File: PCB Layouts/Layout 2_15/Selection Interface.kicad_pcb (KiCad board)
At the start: 4 copper layers, 110 x 90 mm, 127 parts, among them P13 CONN_01X10, P18 CONN_02X05, P19 CONN_02X05, P21 CONN_02X05, P6 CONN_02X10, P8 CONN_02X04, U1 CY8C42_(48_TQFP), U2 CY8C42_(48_TQFP), U3 CY8C58_(100_TQFP), U3_USB USB_2.0_B, U4 CY8C42_(48_TQFP), U5 68_PLCC_Socket_(8468-21B1-RK-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, U6 CY8C42_(48_TQFP), U7 CY8C58_(100_TQFP), U7_USB USB_2.0_B

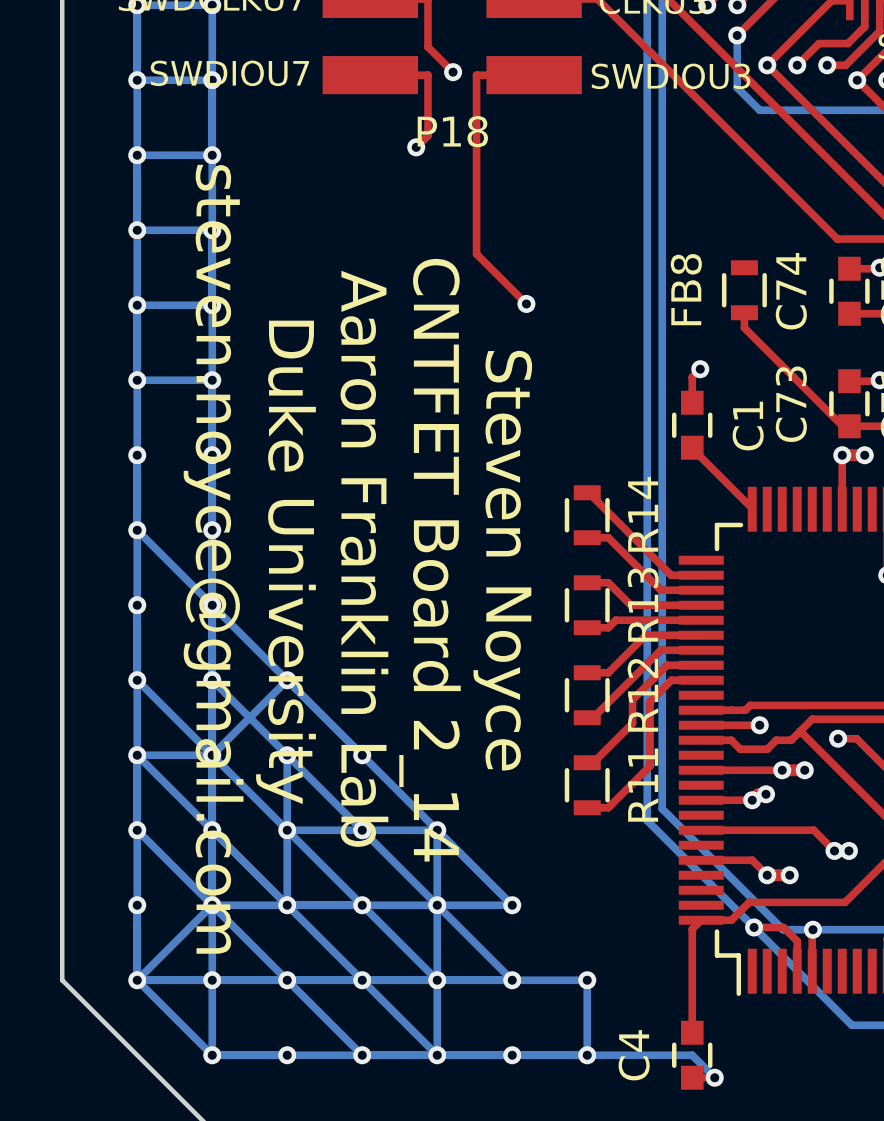
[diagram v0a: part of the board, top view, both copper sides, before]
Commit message: Loaded and updated PCB Layout 2_15 for the first time
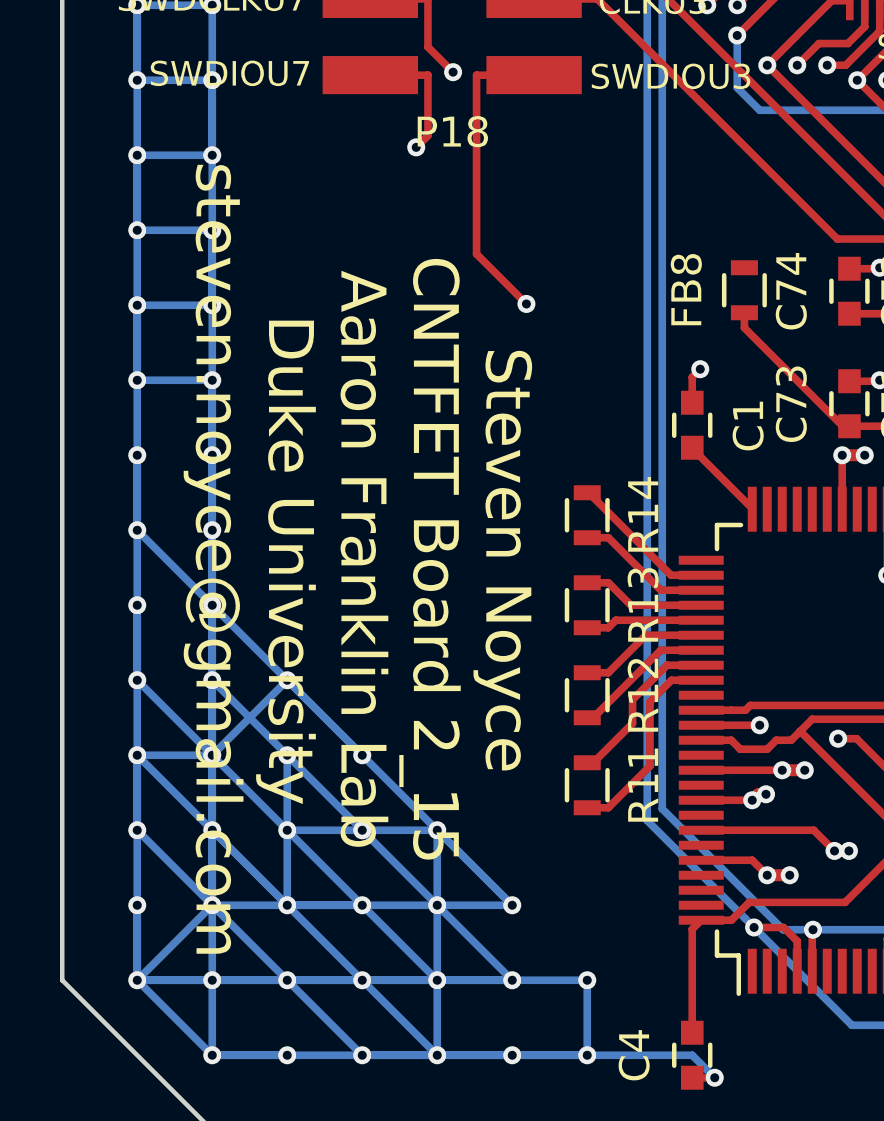
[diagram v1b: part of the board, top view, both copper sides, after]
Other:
- board text added: "Steven Noyce CNTFET Board 2_15 Aaron Franklin Lab Duke University steven.noyce@gmail.com"
- board text removed: "Steven Noyce CNTFET Board 2_14 Aaron Franklin Lab Duke University steven.noyce@gmail.com"
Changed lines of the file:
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@@
-(kicad_pcb (version 4) (host pcbnew 4.0.5)
+(kicad_pcb (version 20171130) (host pcbnew "(5.0.0-3-g5ebb6b6)")
   (general
-    (links 505)
-    (no_connects 0)
-    (area 97.599999 -10.100001 283.600001 200.100001)
     (thickness 1.6)
     (drawings 129)
@@
       (layerselection 0x010f8_80000007)
       (usegerberextensions false)
+      (usegerberattributes false)
+      (usegerberadvancedattributes false)
+      (creategerberjobfile false)
       (excludeedgelayer true)
       (linewidth 0.100000)
@@
       (hpglpennumber 1)
       (hpglpenspeed 20)
-      (hpglpendiameter 15)
-      (hpglpenoverlay 2)
+      (hpglpendiameter 15.000000)
       (psnegative false)
       (psa4output false)
@@
       (drillshape 0)
       (scaleselection 1)
-      (outputdirectory Gerbers/))
+      (outputdirectory "Gerbers/"))
   )
   (net 0 "")
@@
     (solder_paste_ratio -0.16)
     (attr smd)
-    (fp_text reference U2 (at -5.9 0 360) (layer F.SilkS)
+    (fp_text reference U2 (at -5.9 0) (layer F.SilkS)
       (effects (font (size 1 1) (thickness 0.15)))
     )
@@
     (solder_mask_margin 0.2)
     (solder_paste_margin -0.1)
-    (fp_text reference P6 (at -13.31 0 360) (layer F.SilkS)
+    (fp_text reference P6 (at -13.31 0) (layer F.SilkS)
       (effects (font (size 1 1) (thickness 0.15)))
     )
@@
     (solder_mask_margin 0.2)
     (solder_paste_margin -0.1)
-    (fp_text reference P19 (at 7 0 360) (layer F.SilkS)
+    (fp_text reference P19 (at 7 0) (layer F.SilkS)
       (effects (font (size 1 1) (thickness 0.15)))
     )
@@
     (solder_mask_margin 0.2)
     (solder_paste_margin -0.1)
-    (fp_text reference P21 (at -7 0 360) (layer F.SilkS)
+    (fp_text reference P21 (at -7 0) (layer F.SilkS)
       (effects (font (size 1 1) (thickness 0.15)))
     )
@@
     (solder_mask_margin 0.2)
     (solder_paste_margin -0.1)
-    (fp_text reference P13 (at -13.23 0 360) (layer F.SilkS)
+    (fp_text reference P13 (at -13.23 0) (layer F.SilkS)
       (effects (font (size 1 1) (thickness 0.15)))
     )
@@
   (gr_line (start 206 159) (end 194 159) (angle 90) (layer Edge.Cuts) (width 0.15))
   (gr_line (start 207 160) (end 206 159) (angle 90) (layer Edge.Cuts) (width 0.15))
-  (gr_text "Steven Noyce\nCNTFET Board 2_14\nAaron Franklin Lab\nDuke University\nsteven.noyce@gmail.com" (at 160 141 270) (layer F.SilkS)
+  (gr_text "Steven Noyce\nCNTFET Board 2_15\nAaron Franklin Lab\nDuke University\nsteven.noyce@gmail.com" (at 160 141 270) (layer F.SilkS)
     (effects (font (size 1.5 1.5) (thickness 0.3)))
   )

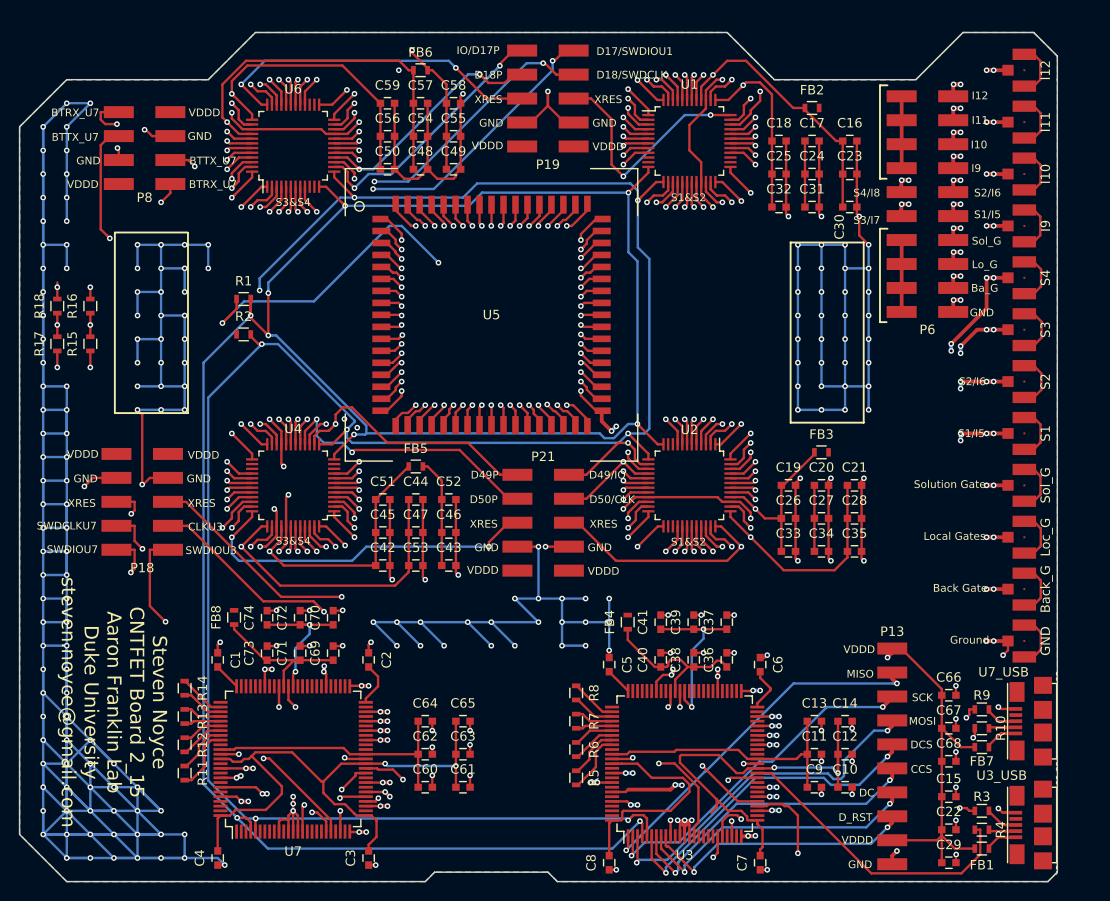
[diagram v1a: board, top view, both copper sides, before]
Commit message: Regenerated and loaded the netlist for Layout 2_15. All components are now switched over to the most up-to-date footprints. Added mounting holes to the schematic and layout. The design is now ready for a more significant overhaul, so will likely be creating a new version soon.
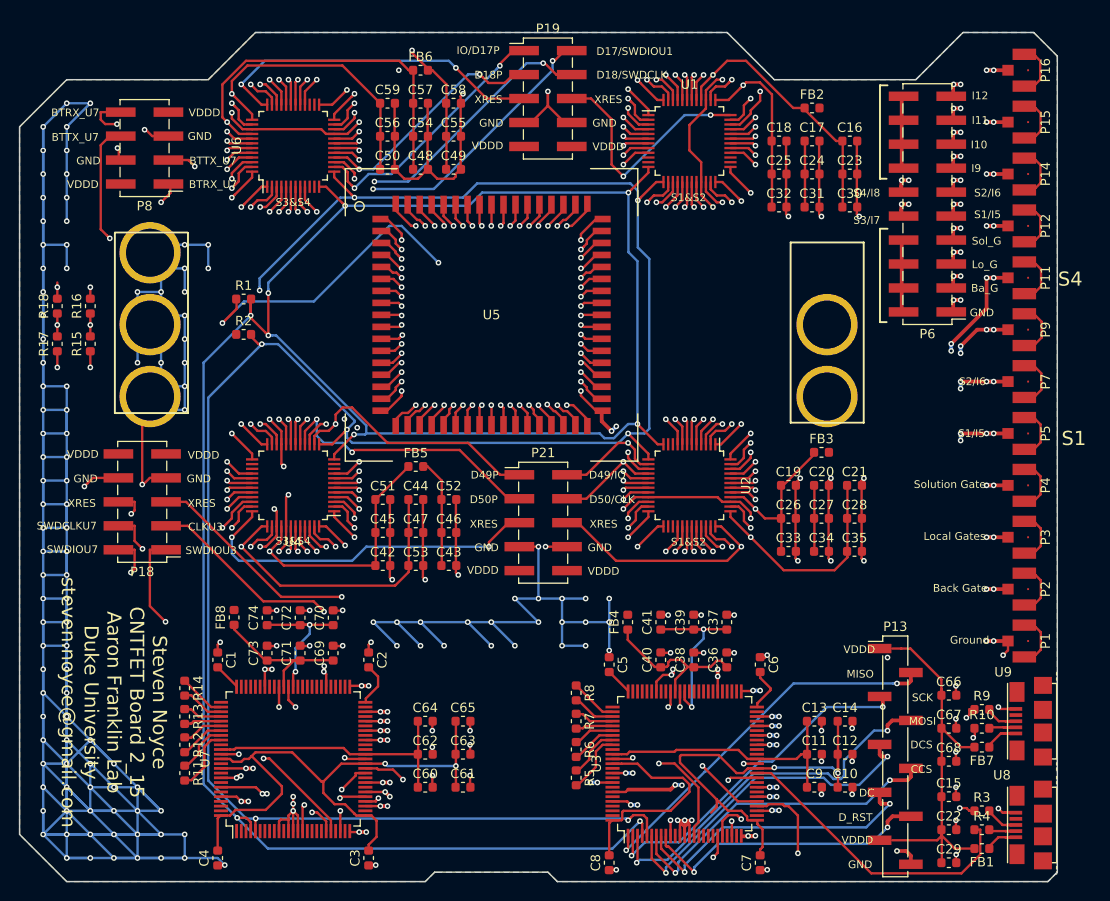
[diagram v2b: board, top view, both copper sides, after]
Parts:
- removed Back_G, GND, I10, I11, I12, I9, Loc_G, S1, S2, S3, S4, Sol_G: CONN_01X02, NoyceLibrary:IPEX_Connector_SMD_(RECE.20279.001E.01)
- removed U3_USB, U7_USB: USB_2.0_B, NoyceLibrary:Micro_USB_2.0_B_SMD(10118192-0001LF)
- added MH1: MountingHole, Custom_Footprint_Library:MountingHole_5.1mm, F.Cu at (163.8, 92.7)
- added MH2: MountingHole, Custom_Footprint_Library:MountingHole_5.1mm, F.Cu at (163.8, 100.3)
- added MH3: MountingHole, Custom_Footprint_Library:MountingHole_5.1mm, F.Cu at (163.8, 108.0)
- added MH5: MountingHole, Custom_Footprint_Library:MountingHole_5.1mm, F.Cu at (236.2, 103.5)
- added MH6: MountingHole, Custom_Footprint_Library:MountingHole_5.1mm, F.Cu at (236.2, 108.6)
- added P1: CONN_01X02, Custom_Footprint_Library:IPEX_Connector_SMD_(RECE.20279.001E.01), F.Cu at (255.2, 134.5)
- added P11: CONN_01X02, Custom_Footprint_Library:IPEX_Connector_SMD_(RECE.20279.001E.01), F.Cu at (255.2, 96.0)
- added P12: CONN_01X02, Custom_Footprint_Library:IPEX_Connector_SMD_(RECE.20279.001E.01), F.Cu at (255.2, 90.5)
- added P14: CONN_01X02, Custom_Footprint_Library:IPEX_Connector_SMD_(RECE.20279.001E.01), F.Cu at (255.2, 85.0)
- added P15: CONN_01X02, Custom_Footprint_Library:IPEX_Connector_SMD_(RECE.20279.001E.01), F.Cu at (255.2, 79.5)
- added P16: CONN_01X02, Custom_Footprint_Library:IPEX_Connector_SMD_(RECE.20279.001E.01), F.Cu at (255.2, 74.0)
- added P2: CONN_01X02, Custom_Footprint_Library:IPEX_Connector_SMD_(RECE.20279.001E.01), F.Cu at (255.2, 129.0)
- added P3: CONN_01X02, Custom_Footprint_Library:IPEX_Connector_SMD_(RECE.20279.001E.01), F.Cu at (255.2, 123.5)
- added P4: CONN_01X02, Custom_Footprint_Library:IPEX_Connector_SMD_(RECE.20279.001E.01), F.Cu at (255.2, 118.0)
- added P5: CONN_01X02, Custom_Footprint_Library:IPEX_Connector_SMD_(RECE.20279.001E.01), F.Cu at (255.2, 112.5)
- added P7: CONN_01X02, Custom_Footprint_Library:IPEX_Connector_SMD_(RECE.20279.001E.01), F.Cu at (255.2, 107.0)
- added P9: CONN_01X02, Custom_Footprint_Library:IPEX_Connector_SMD_(RECE.20279.001E.01), F.Cu at (255.2, 101.5)
- added U8: USB_2.0_B, Custom_Footprint_Library:Micro_USB_2.0_B_SMD(10118192-0001LF), F.Cu at (258.5, 154.0)
- added U9: USB_2.0_B, Custom_Footprint_Library:Micro_USB_2.0_B_SMD(10118192-0001LF), F.Cu at (258.5, 143.0)
- C1, C10, C11, C12, C13, C14, C15, C16, C17, C18, C19, C2, C20, C21, C22, C23, C24, C25, C26, C27, C28, C29, C3, C30, C31, C32, C33, C34, C35, C36, C37, C38, C39, C4, C40, C41, C42, C43, C44, C45, C46, C47, C48, C49, C5, C50, C51, C52, C53, C54, C55, C56, C57, C58, C59, C6, C60, C61, C62, C63, C64, C65, C66, C67, C68, C69, C7, C70, C71, C72, C73, C74, C8, C9: footprint Capacitors_SMD:C_0603 -> Capacitor_SMD:C_0603_1608Metric
- FB1, FB2, FB3, FB4, FB5, FB6, FB7, FB8, R1, R10, R11, R12, R13, R14, R15, R16, R17, R18, R2, R3, R4, R5, R6, R7, R8, R9: footprint Resistors_SMD:R_0603 -> Resistor_SMD:R_0603_1608Metric
- P13: footprint NoyceLibrary:Headers_SMD_1x10_(cut_95157-240LF) -> Connector_PinHeader_2.54mm:PinHeader_1x10_P2.54mm_Vertical_SMD_Pin1Left
- P18, P19, P21: footprint NoyceLibrary:Headers_SMD_2x5_(cut_95157-240LF) -> Connector_PinHeader_2.54mm:PinHeader_2x05_P2.54mm_Vertical_SMD
- P6: footprint NoyceLibrary:Headers_SMD_2x10_(cut_95157-240LF) -> Connector_PinHeader_2.54mm:PinHeader_2x10_P2.54mm_Vertical_SMD
- P8: footprint NoyceLibrary:Headers_SMD_2x4_(cut_95157-240LF) -> Connector_PinHeader_2.54mm:PinHeader_2x04_P2.54mm_Vertical_SMD
- U1, U2, U4, U6: footprint Housings_QFP:TQFP-48_7x7mm_Pitch0.5mm -> Package_QFP:TQFP-48_7x7mm_P0.5mm
- U3, U7: footprint Housings_QFP:TQFP-100_14x14mm_Pitch0.5mm -> Package_QFP:TQFP-100_14x14mm_P0.5mm
- U5: footprint NoyceLibrary:68_PLCC_Socket_(8468-21B1-RK-TP) -> Custom_Footprint_Library:68_PLCC_Socket_(8468-21B1-RK-TP)
- moved P13 0.32 mm to (242.8, 146.7), turned to 0 degrees
- turned P18 to 180 degrees
- turned P19 to 0 degrees
- turned P21 to 0 degrees
- turned P6 to 180 degrees
- turned P8 to 180 degrees
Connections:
- U1 pad 10: (no net) -> Net-(U1-Pad10)
- U1 pad 11: (no net) -> Net-(U1-Pad11)
- U1 pad 26: (no net) -> Net-(U1-Pad26)
- U1 pad 27: (no net) -> Net-(U1-Pad27)
- U2 pad 10: (no net) -> Net-(U2-Pad10)
- U2 pad 11: (no net) -> Net-(U2-Pad11)
- U2 pad 26: (no net) -> Net-(U2-Pad26)
- U2 pad 27: (no net) -> Net-(U2-Pad27)
- U3 pad 11: (no net) -> Net-(U3-Pad11)
- U3 pad 16: (no net) -> Net-(U3-Pad16)
- U3 pad 17: (no net) -> Net-(U3-Pad17)
- U3 pad 18: (no net) -> Net-(U3-Pad18)
- U3 pad 19: (no net) -> Net-(U3-Pad19)
- U3 pad 22: (no net) -> Net-(U3-Pad22)
- U3 pad 24: (no net) -> Net-(U3-Pad24)
- U3 pad 27: (no net) -> Net-(U3-Pad27)
- U3 pad 32: (no net) -> Net-(U3-Pad32)
- U3 pad 34: (no net) -> Net-(U3-Pad34)
- U3 pad 40: (no net) -> Net-(U3-Pad40)
- U3 pad 41: (no net) -> Net-(U3-Pad41)
- U3 pad 43: (no net) -> Net-(U3-Pad43)
- U3 pad 45: (no net) -> Net-(U3-Pad45)
- U3 pad 47: (no net) -> Net-(U3-Pad47)
- U3 pad 49: (no net) -> Net-(U3-Pad49)
- U3 pad 52: (no net) -> Net-(U3-Pad52)
- U3 pad 53: (no net) -> Net-(U3-Pad53)
- U3 pad 54: (no net) -> Net-(U3-Pad54)
- U3 pad 55: (no net) -> Net-(U3-Pad55)
- U3 pad 57: (no net) -> Net-(U3-Pad57)
- U3 pad 58: (no net) -> Net-(U3-Pad58)
- U3 pad 59: (no net) -> Net-(U3-Pad59)
- U3 pad 60: (no net) -> Net-(U3-Pad60)
- U3 pad 61: (no net) -> Net-(U3-Pad61)
- U3 pad 62: (no net) -> Net-(U3-Pad62)
- U3 pad 67: (no net) -> Net-(U3-Pad67)
- U3 pad 68: (no net) -> Net-(U3-Pad68)
- U3 pad 70: (no net) -> Net-(U3-Pad70)
- U3 pad 71: (no net) -> Net-(U3-Pad71)
- U3 pad 72: (no net) -> Net-(U3-Pad72)
- U3 pad 73: (no net) -> Net-(U3-Pad73)
- U3 pad 74: (no net) -> Net-(U3-Pad74)
- U3 pad 76: (no net) -> Net-(U3-Pad76)
- U3 pad 85: (no net) -> Net-(U3-Pad85)
- U3 pad 89: (no net) -> Net-(U3-Pad89)
- U3 pad 91: (no net) -> Net-(U3-Pad91)
- U3 pad 93: (no net) -> Net-(U3-Pad93)
- U3 pad 95: (no net) -> Net-(U3-Pad95)
- U3 pad 97: (no net) -> Net-(U3-Pad97)
- U3 pad 98: (no net) -> Net-(U3-Pad98)
- U3 pad 99: (no net) -> Net-(U3-Pad99)
- U4 pad 10: (no net) -> Net-(U4-Pad10)
- U4 pad 11: (no net) -> Net-(U4-Pad11)
- U4 pad 26: (no net) -> Net-(U4-Pad26)
- U4 pad 27: (no net) -> Net-(U4-Pad27)
- U6 pad 10: (no net) -> Net-(U6-Pad10)
- U6 pad 11: (no net) -> Net-(U6-Pad11)
- U6 pad 26: (no net) -> Net-(U6-Pad26)
- U6 pad 27: (no net) -> Net-(U6-Pad27)
- U7 pad 1: (no net) -> Net-(U7-Pad1)
- U7 pad 11: (no net) -> Net-(U7-Pad11)
- U7 pad 16: (no net) -> Net-(U7-Pad16)
- U7 pad 17: (no net) -> Net-(U7-Pad17)
- U7 pad 18: (no net) -> Net-(U7-Pad18)
- U7 pad 19: (no net) -> Net-(U7-Pad19)
- U7 pad 2: (no net) -> Net-(U7-Pad2)
- U7 pad 22: (no net) -> Net-(U7-Pad22)
- U7 pad 24: (no net) -> Net-(U7-Pad24)
- U7 pad 27: (no net) -> Net-(U7-Pad27)
- U7 pad 3: (no net) -> Net-(U7-Pad3)
- U7 pad 32: (no net) -> Net-(U7-Pad32)
- U7 pad 34: (no net) -> Net-(U7-Pad34)
- U7 pad 40: (no net) -> Net-(U7-Pad40)
- U7 pad 41: (no net) -> Net-(U7-Pad41)
- U7 pad 43: (no net) -> Net-(U7-Pad43)
- U7 pad 45: (no net) -> Net-(U7-Pad45)
- U7 pad 47: (no net) -> Net-(U7-Pad47)
- U7 pad 49: (no net) -> Net-(U7-Pad49)
- U7 pad 52: (no net) -> Net-(U7-Pad52)
- U7 pad 53: (no net) -> Net-(U7-Pad53)
- U7 pad 54: (no net) -> Net-(U7-Pad54)
- U7 pad 55: (no net) -> Net-(U7-Pad55)
- U7 pad 57: (no net) -> Net-(U7-Pad57)
- U7 pad 58: (no net) -> Net-(U7-Pad58)
- U7 pad 59: (no net) -> Net-(U7-Pad59)
- U7 pad 6: (no net) -> Net-(U7-Pad6)
- U7 pad 60: (no net) -> Net-(U7-Pad60)
- U7 pad 61: (no net) -> Net-(U7-Pad61)
- U7 pad 62: (no net) -> Net-(U7-Pad62)
- U7 pad 67: (no net) -> Net-(U7-Pad67)
- U7 pad 68: (no net) -> Net-(U7-Pad68)
- U7 pad 7: (no net) -> Net-(U7-Pad7)
- U7 pad 70: (no net) -> Net-(U7-Pad70)
- U7 pad 71: (no net) -> Net-(U7-Pad71)
- U7 pad 72: (no net) -> Net-(U7-Pad72)
- U7 pad 73: (no net) -> Net-(U7-Pad73)
- U7 pad 74: (no net) -> Net-(U7-Pad74)
- U7 pad 76: (no net) -> Net-(U7-Pad76)
- U7 pad 8: (no net) -> Net-(U7-Pad8)
- U7 pad 85: (no net) -> Net-(U7-Pad85)
- U7 pad 89: (no net) -> Net-(U7-Pad89)
- U7 pad 9: (no net) -> Net-(U7-Pad9)
- U7 pad 91: (no net) -> Net-(U7-Pad91)
- U7 pad 93: (no net) -> Net-(U7-Pad93)
- U7 pad 95: (no net) -> Net-(U7-Pad95)
- U7 pad 97: (no net) -> Net-(U7-Pad97)
- U7 pad 98: (no net) -> Net-(U7-Pad98)
- U7 pad 99: (no net) -> Net-(U7-Pad99)
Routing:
- net GND: track 957.2 -> 869.8 mm, vias 259 -> 227
- net DisplayMOSI: track 37.9 -> 39.9 mm
- net DisplayReset: track 29.3 -> 31.3 mm
- net CardCS: track 33.4 -> 35.3 mm
- net DisplayMISO: track 39.0 -> 40.1 mm
- net DisplayDataOrCommand: track 31.3 -> 32.2 mm
- net DisplayCS: track 35.6 -> 36.1 mm
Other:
- board text added: "S1"
- board text added: "S4"

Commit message: Fixed swapping of Back gate and solution gate in Layout 2_15
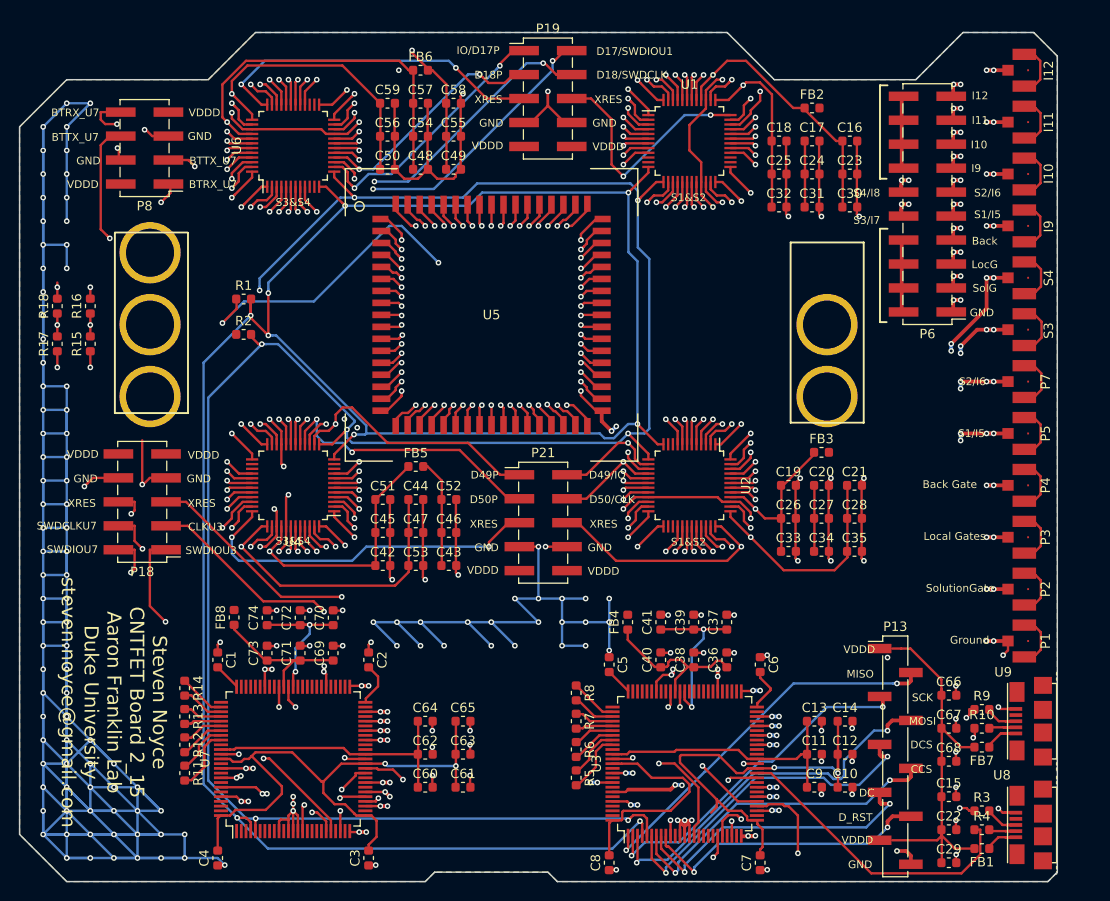
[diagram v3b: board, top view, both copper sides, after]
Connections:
- P2 pad 1: BackGate -> I2
- P4 pad 1: I4 -> BackGate
- P6 pad 3: BackGate -> I2
- P6 pad 7: I4 -> BackGate
- U3 pad 25: BackGate -> I2
- U3 pad 31: I4 -> BackGate
- U5 pad 34: BackGate -> I2
- U5 pad 68: I4 -> BackGate
- U7 pad 25: BackGate -> I2
- U7 pad 31: I4 -> BackGate
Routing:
- net I2: track 0.00 -> 178.4 mm, vias 0 -> 9
- net I4: track 175.3 -> 0.00 mm, vias 11 -> 0
- net GND: track 869.8 -> 801.3 mm, vias 227 -> 201
- net BackGate: track 178.4 -> 175.3 mm, vias 9 -> 11
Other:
- board text added: "Back"
- board text added: "LocG"
- board text added: "S3"
- board text added: "SolG"
- board text added: "SolutionGate"
- board text removed: "Ba_G"
- board text removed: "Lo_G"
- board text removed: "S1"
- board text removed: "Sol_G"
- board text removed: "Solution Gate"
